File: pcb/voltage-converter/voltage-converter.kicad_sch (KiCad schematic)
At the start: 20 parts, among them J4 Conn_01x02, J8 I2C, U3 R-78C3.3-1.0

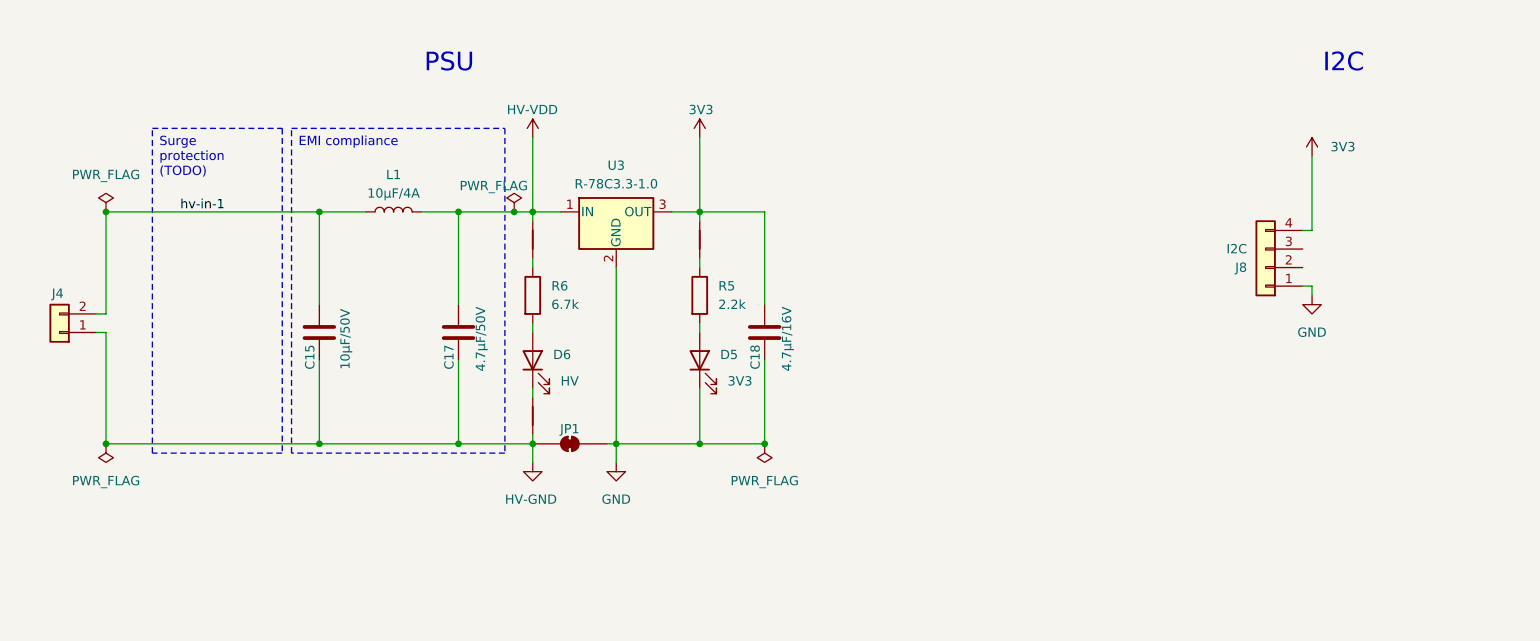
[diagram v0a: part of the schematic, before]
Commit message: Making converter PCB larger.
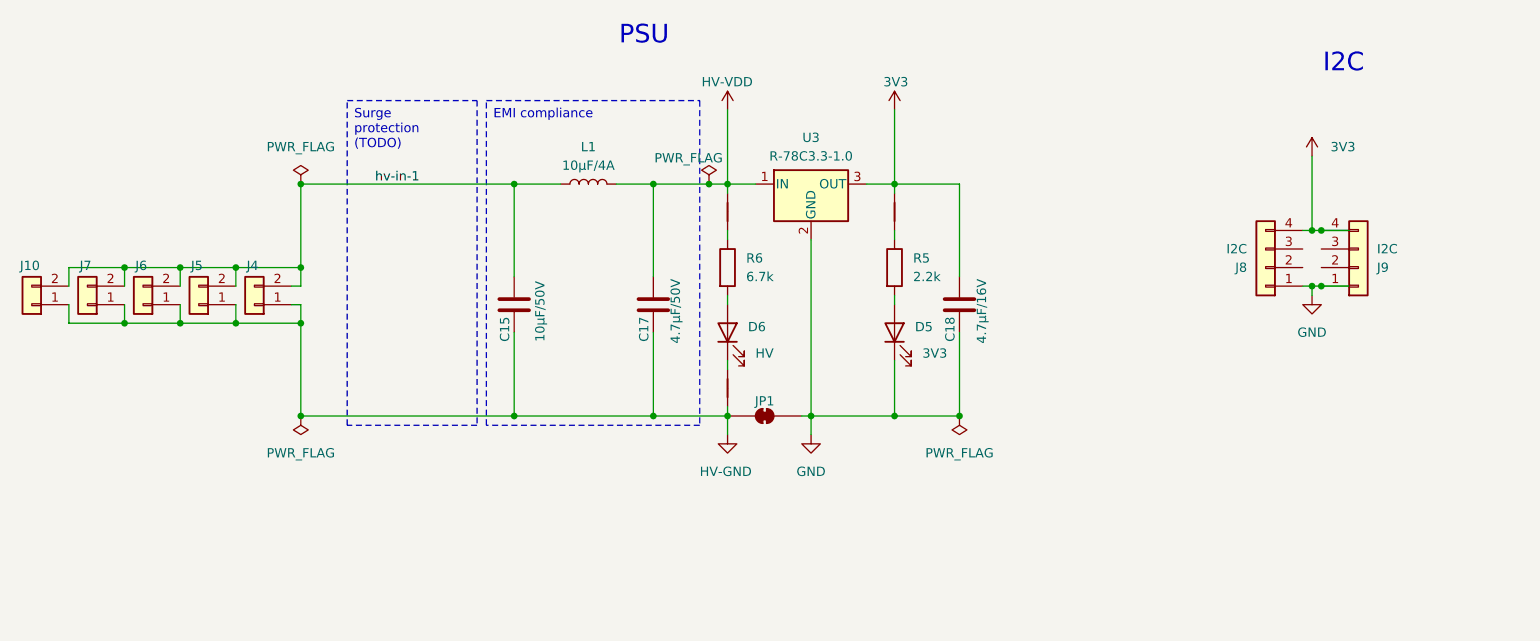
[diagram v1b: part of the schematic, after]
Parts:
- added J10, J5, J6, J7: Conn_01x02, Connector_JST:JST_VH_B2P-VH_1x02_P3.96mm_Vertical, symbol Connector_Generic:Conn_01x02
- added J9: I2C, Connector_JST:JST_XH_B4B-XH-A_1x04_P2.50mm_Vertical, symbol Connector_Generic:Conn_01x04
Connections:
- net 3V3: now also J9.4 (Pin_4)
- net GND: now also J9.1 (Pin_1)
- net HV-GND: now also J10.1 (Pin_1), J5.1 (Pin_1), J6.1 (Pin_1), J7.1 (Pin_1)
- net hv-in-1: now also J10.2 (Pin_2), J5.2 (Pin_2), J6.2 (Pin_2), J7.2 (Pin_2)
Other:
- moved on the sheet: C15, C17, C18, D5, D6, J4, JP1, L1, R5, R6, U3

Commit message: Preparing voltage converter for fabrication.
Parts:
- J6: renamed from J8; value I2C -> (none)
- J7: renamed from J9; value I2C -> (none)
- renumbered C15 to C1, C17 to C2, C18 to C3, D6 to D1, D5 to D2, J10 to J1, J7 to J2, J6 to J3, J5 to J4, J4 to J5, NT2 to NT1, NT3 to NT2, NT4 to NT3, R6 to R1, R5 to R2, U3 to U1
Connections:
- no-connect marks 0 -> 4
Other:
- note added: "Just an expander for high voltage to plug multiple boards in"
- note added: "Low power ports"
- note removed: "I2C"
- moved on the sheet: C1, C2, C3, D1, D2, J1, J2, J3, J4, J5, J6, J7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
